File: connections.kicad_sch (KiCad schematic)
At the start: 37 parts, among them J1 Conn_01x01_Pin, J2 Conn_01x04_Pin, Q1 BSS138, Q2 BSS138

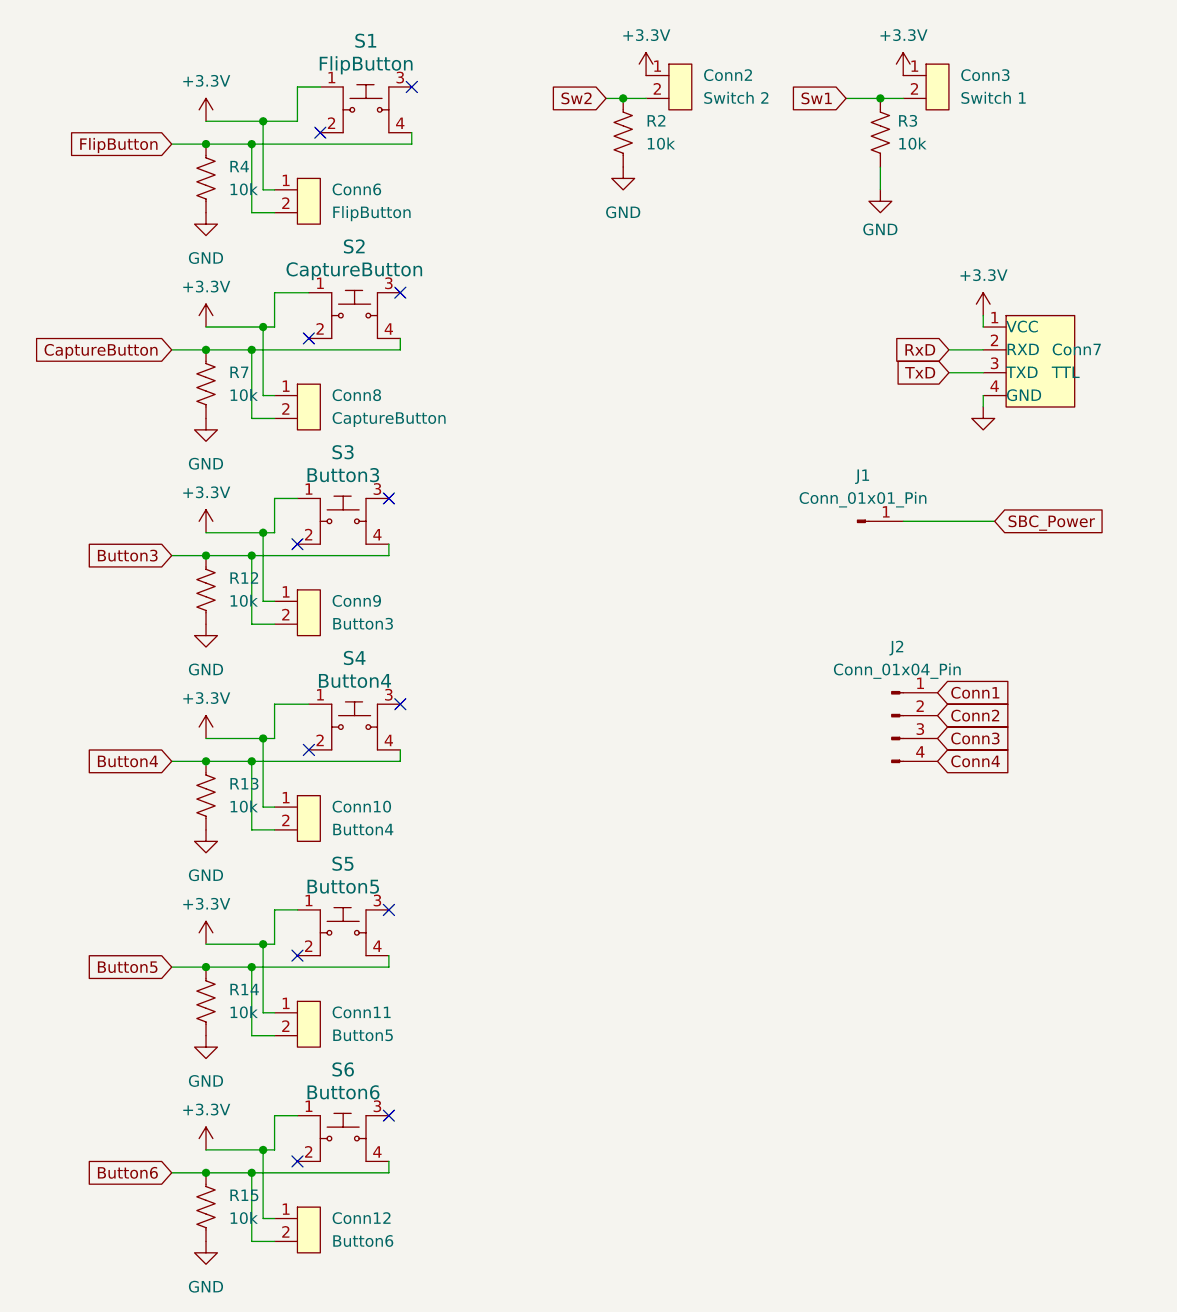
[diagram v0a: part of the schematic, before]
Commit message: Removed motor and added A4988
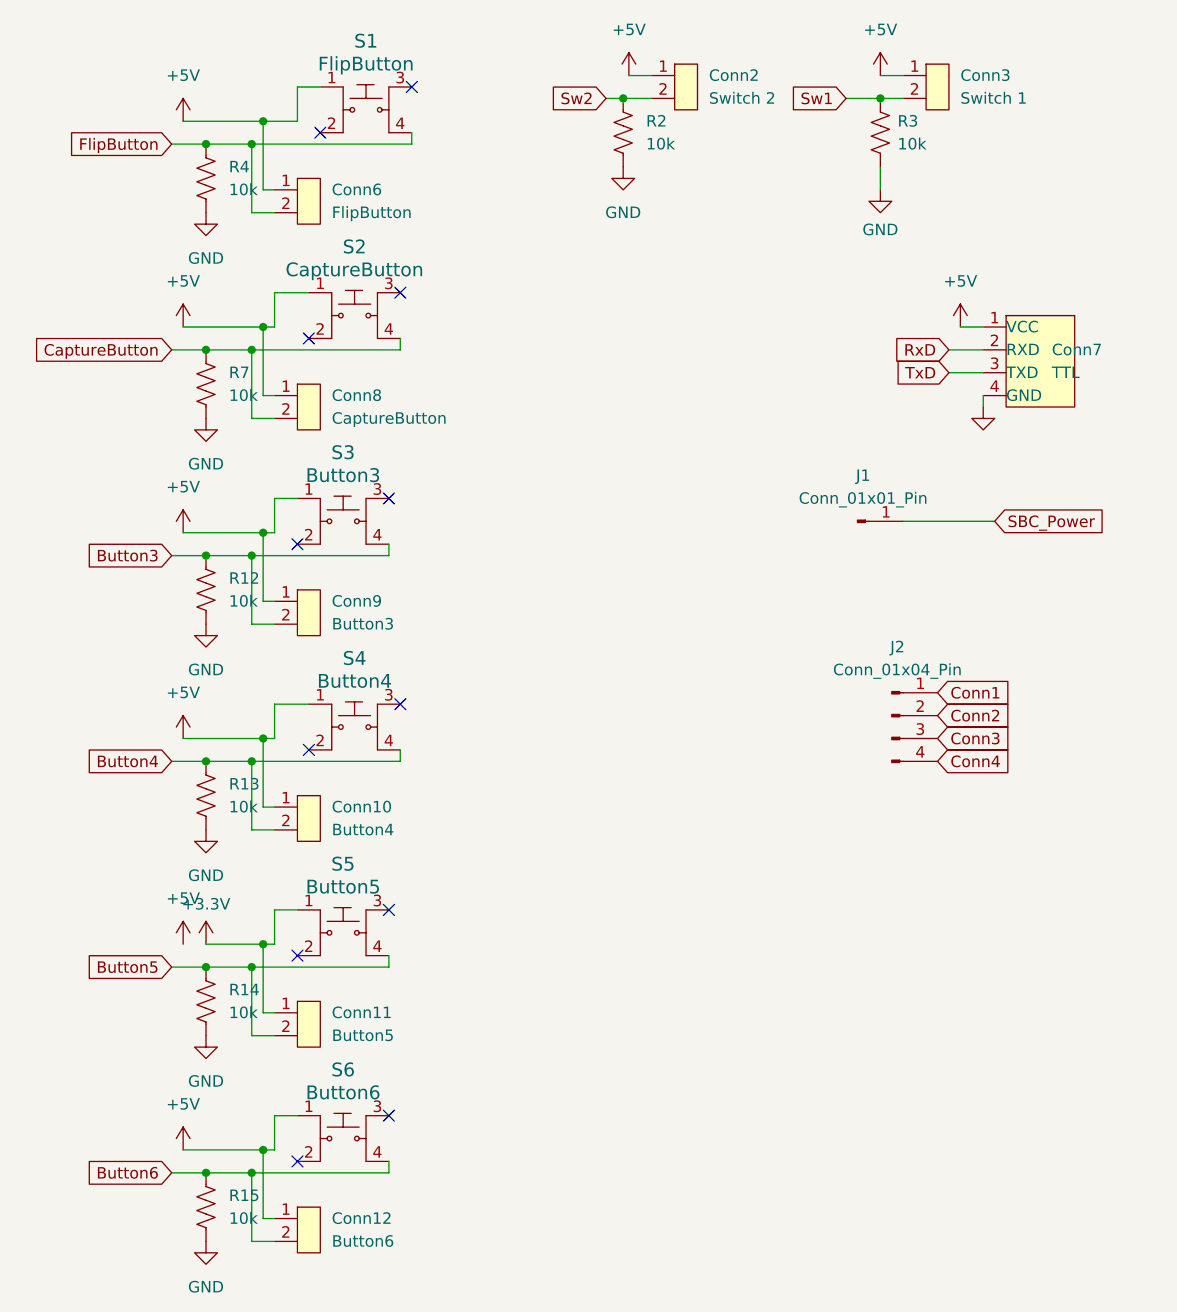
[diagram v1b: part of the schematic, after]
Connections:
- net +3.3V: no longer Conn10.1 (Pin_1), Conn12.1 (Pin_1), Conn2.1 (Pin_1), Conn3.1 (Pin_1), Conn6.1 (Pin_1), Conn7.1 (VCC), Conn8.1 (Pin_1), Conn9.1 (Pin_1), S1.1, S2.1, S3.1, S4.1, S6.1
- net +5V: now also Conn10.1 (Pin_1), Conn12.1 (Pin_1), Conn2.1 (Pin_1), Conn3.1 (Pin_1), Conn6.1 (Pin_1), Conn7.1 (VCC), Conn8.1 (Pin_1), Conn9.1 (Pin_1), S1.1, S2.1, S3.1, S4.1, S6.1
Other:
- moved on the sheet: Conn2

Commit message: Added motor driver
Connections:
- net +3.3V: no longer Conn11.1 (Pin_1), S5.1
- net +5V: now also Conn11.1 (Pin_1), S5.1
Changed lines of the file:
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@@
 	(wire
 		(pts
-			(xy 44.45 123.19) (xy 38.1 123.19)
-		)
-		(stroke
-			(width 0)
-			(type default)
-		)
-	)
-	(wire
-		(pts
 			(xy 43.18 80.01) (xy 43.18 87.63)
 		)
@@
 	(wire
 		(pts
+			(xy 38.1 123.19) (xy 44.45 123.19)
+		)
+		(stroke
+			(width 0)
+			(type default)
+		)
+	)
+	(wire
+		(pts
 			(xy 43.18 148.59) (xy 43.18 156.21)
 		)
@@
 	(symbol
 		(lib_id "power:+5V")
-		(at 35.56 123.19 0)
+		(at 38.1 123.19 0)
 		(unit 1)
 		(exclude_from_sim no)
@@
 		(fields_autoplaced yes)
 		(property "Reference" "#PWR057"
-			(at 35.56 127 0)
+			(at 38.1 127 0)
 			(effects
 				(font
@@
 		)
 		(property "Value" "+5V"
-			(at 35.56 118.11 0)
+			(at 38.1 118.11 0)
 			(effects
 				(font
@@
 		)
 		(property "Footprint" ""
-			(at 35.56 123.19 0)
+			(at 38.1 123.19 0)
 			(effects
 				(font
@@
 		)
 		(property "Datasheet" ""
-			(at 35.56 123.19 0)
+			(at 38.1 123.19 0)
 			(effects
 				(font
@@
 		)
 		(property "Description" ""
-			(at 35.56 123.19 0)
+			(at 38.1 123.19 0)
 			(effects
 				(font
@@
 					(unit 1)
 				)
-			)
-		)
-	)
-	(symbol
-		(lib_id "power:+3.3V")
-		(at 38.1 123.19 0)
-		(unit 1)
-		(exclude_from_sim no)
-		(in_bom yes)
-		(on_board yes)
-		(dnp no)
-		(fields_autoplaced yes)
-		(property "Reference" "#PWR030"
-			(at 38.1 127 0)
-			(effects
-				(font
-					(size 1.27 1.27)
-				)
-				(hide yes)
-			)
-		)
-		(property "Value" "+3.3V"
-			(at 38.1 118.745 0)
-			(effects
-				(font
-					(size 1.27 1.27)
-				)
-			)
-		)
-		(property "Footprint" ""
-			(at 38.1 123.19 0)
-			(effects
-				(font
-					(size 1.27 1.27)
-				)
-				(hide yes)
-			)
-		)
-		(property "Datasheet" ""
-			(at 38.1 123.19 0)
-			(effects
-				(font
-					(size 1.27 1.27)
-				)
-				(hide yes)
-			)
-		)
-		(property "Description" ""
-			(at 38.1 123.19 0)
-			(effects
-				(font
-					(size 1.27 1.27)
-				)
-				(hide yes)
-			)
-		)
-		(pin "1"
-		)
-		(instances
-			(project "Scout_Board"
-				(path "/e58a9779-147f-4c0c-a745-6e9bc8ec0357/1c50300d-eb18-4ae0-a965-4e91fdf6ec14"
-					(reference "#PWR030")
-					(unit 1)
-				)

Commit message: MID CHANGES
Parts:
- removed Conn2: Switch 2, Downloaded_footprints:CONN_B2B-ZRLFSN_JST, symbol Scout_library:B2B_VERT_1.5MM
- removed Conn3: Switch 1, Downloaded_footprints:CONN_B2B-ZRLFSN_JST, symbol Scout_library:B2B_VERT_1.5MM
- removed Conn4: TopLights, Downloaded_footprints:CONN_B2B-ZRLFSN_JST, symbol Scout_library:B2B_VERT_1.5MM
- removed Conn5: BottomLights, Downloaded_footprints:CONN_B2B-ZRLFSN_JST, symbol Scout_library:B2B_VERT_1.5MM
- added J10: P8, symbol Connector_Generic:Conn_02x13_Odd_Even
- added J7: Conn_02x07_Odd_Even, symbol Connector_Generic:Conn_02x07_Odd_Even
- added J9: P9, symbol Connector_Generic:Conn_02x13_Odd_Even
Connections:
- net +12V: now also J7.11 (Pin_11), J7.7 (Pin_7)
- net +5V: now also J7.3 (Pin_3), J7.4 (Pin_4)
- net Sw1: now also R2.1, J7.1 (Pin_1); no longer R3.1
- net Sw2: now also R3.1, J7.2 (Pin_2); no longer R2.1
- net BLa: now reaches MOSFET2.2 (D)
- net BLa: now also J7.9 (Pin_9)
- net TLa: now reaches MOSFET1.2 (D)
- net TLa: now also J7.5 (Pin_5)
- new net 1A: J7.8 (Pin_8)
- new net 1B: J7.6 (Pin_6)
- new net 2A: J7.10 (Pin_10)
- new net 2B: J7.12 (Pin_12)
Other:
- moved on the sheet: J2

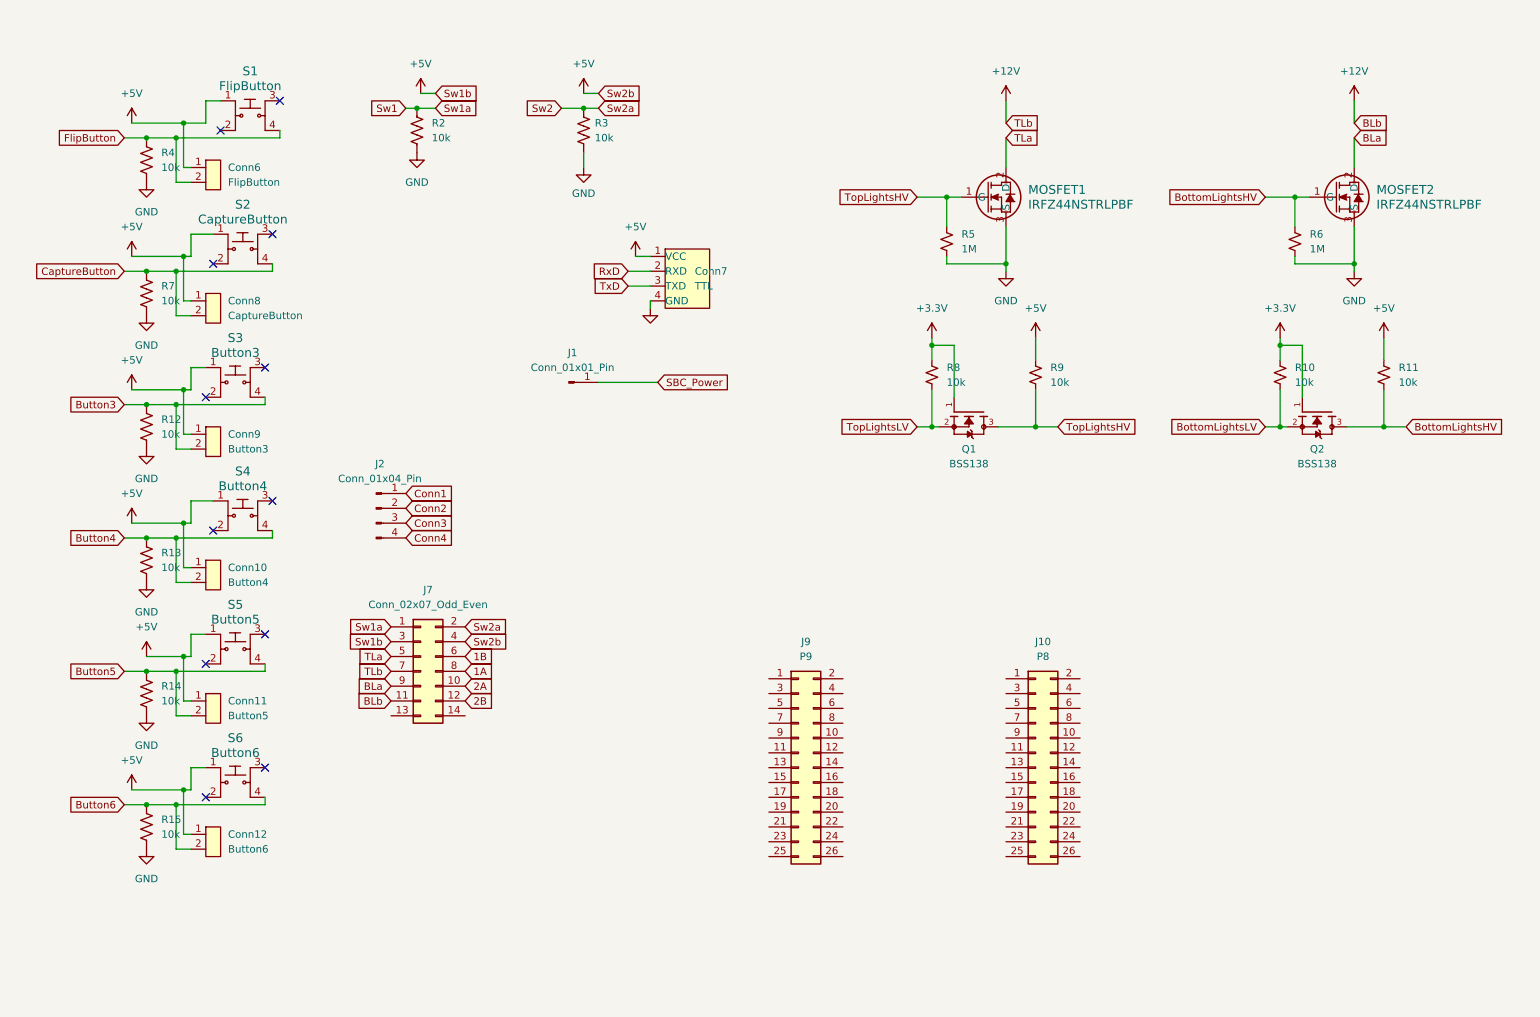
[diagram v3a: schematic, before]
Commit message: power board changes
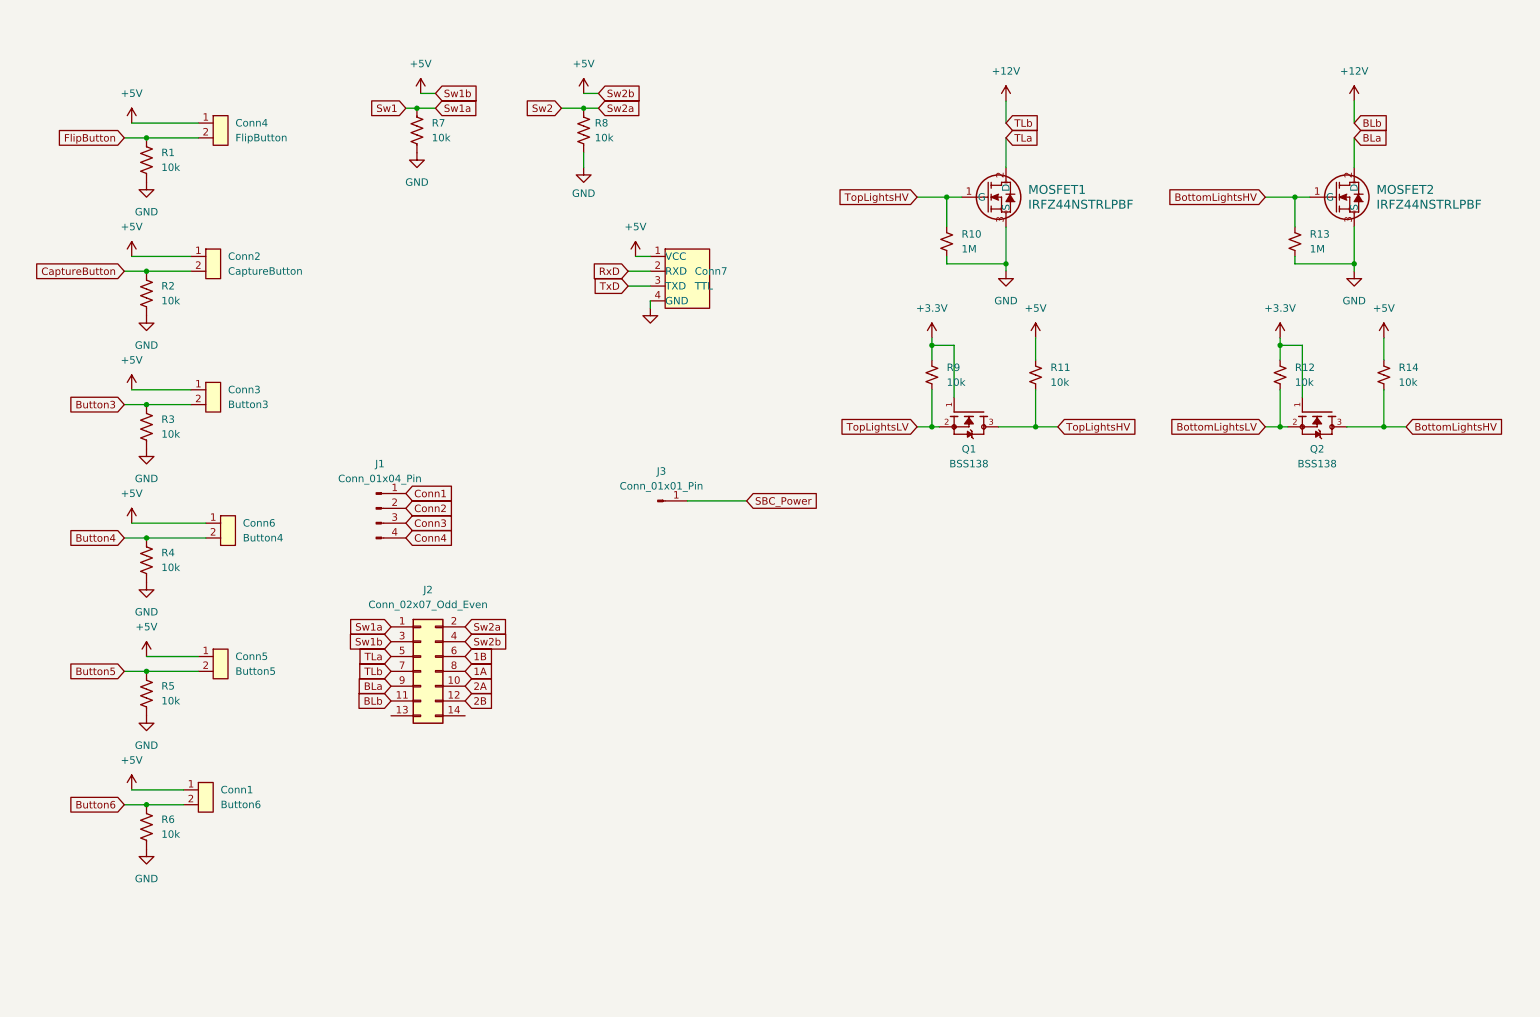
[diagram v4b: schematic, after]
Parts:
- removed J10: P8, symbol Connector_Generic:Conn_02x13_Odd_Even
- removed J9: P9, symbol Connector_Generic:Conn_02x13_Odd_Even
- removed S1: FlipButton, digikey-footprints:Switch_Tactile_SMD_4.5x4.5mm_TL3315NF160Q, symbol dk_Tactile-Switches:TL3315NF160Q
- removed S2: CaptureButton, digikey-footprints:Switch_Tactile_SMD_4.5x4.5mm_TL3315NF160Q, symbol dk_Tactile-Switches:TL3315NF160Q
- removed S3: Button3, digikey-footprints:Switch_Tactile_SMD_4.5x4.5mm_TL3315NF160Q, symbol dk_Tactile-Switches:TL3315NF160Q
- removed S4: Button4, digikey-footprints:Switch_Tactile_SMD_4.5x4.5mm_TL3315NF160Q, symbol dk_Tactile-Switches:TL3315NF160Q
- removed S5: Button5, digikey-footprints:Switch_Tactile_SMD_4.5x4.5mm_TL3315NF160Q, symbol dk_Tactile-Switches:TL3315NF160Q
- removed S6: Button6, digikey-footprints:Switch_Tactile_SMD_4.5x4.5mm_TL3315NF160Q, symbol dk_Tactile-Switches:TL3315NF160Q
- J2: renamed from J7; footprint (none) -> Connector_IDC:IDC-Header_2x07_P2.54mm_Vertical
- renumbered Conn12 to Conn1, Conn8 to Conn2, Conn9 to Conn3, Conn6 to Conn4, Conn11 to Conn5, Conn10 to Conn6, J2 to J1, J1 to J3, R4 to R1, R5 to R10, R9 to R11, R10 to R12, R6 to R13, R11 to R14, R7 to R2, R12 to R3, R13 to R4, R14 to R5, R15 to R6, R2 to R7, R3 to R8, R8 to R9
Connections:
- no-connect marks 12 -> 0
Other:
- moved on the sheet: Conn1, Conn2, Conn3, Conn4, Conn5, Conn6, J3

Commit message: New board test
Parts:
- removed Conn7: TTL, Downloaded_footprints:CONN_B4B-ZRLFSN_JST, symbol Scout_library:B4B_VERT_1.5MM
- Conn1, Conn2, Conn3, Conn4, Conn5, Conn6: footprint Downloaded_footprints:CONN_B2B-ZRLFSN_JST -> Connector_JST:JST_XH_B2B-XH-AM_1x02_P2.50mm_Vertical
- MOSFET1, MOSFET2: footprint Downloaded_footprints:D2PAK_INF -> IRFZ44NSTRLPBF:DPAK254P1524X483-3N
- Q1, Q2: footprint Downloaded_footprints:SOT95P240X111-3N -> BSS138:SOT95P240X111-3N

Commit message: Layout changes
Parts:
- removed J3: Conn_01x01_Pin, Connector_PinHeader_2.54mm:PinHeader_1x01_P2.54mm_Vertical, symbol Connector:Conn_01x01_Pin
- added MOSFET3: IRFZ44NSTRLPBF, IRFZ44NSTRLPBF:DPAK254P1524X483-3N, symbol 2024-05-21_14-07-33:IRFZ44NSTRLPBF
- added Q3: BSS138, BSS138:SOT95P240X111-3N, symbol BSS138:BSS138
- added R29, R31: 10k, Resistor_SMD:R_0603_1608Metric_Pad0.98x0.95mm_HandSolder, symbol Device:R_Small_US
- added R30: 1M, Resistor_SMD:R_0603_1608Metric_Pad0.98x0.95mm_HandSolder, symbol Device:R_Small_US
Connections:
- net +12V: now also J2.5 (Pin_5); no longer J2.11 (Pin_11)
- net +3.3V: now also Q3.1, R29.1
- net +5V: now also R31.1
- net GND: now also MOSFET3.3 (S), R30.2
- net BLa: no longer names the net of J2.9 (Pin_9)
- net BLa: no longer MOSFET2.2 (D)
- net TLa renamed TL-
- net TL-: no longer J2.5 (Pin_5)
- new net BL-: MOSFET2.2 (D)
- new net UV-: MOSFET3.2 (D)
- new net UVLightsHV: MOSFET3.1 (G), Q3.3, R30.1, R31.2
- new net UVLightsLV: Q3.2, R29.2

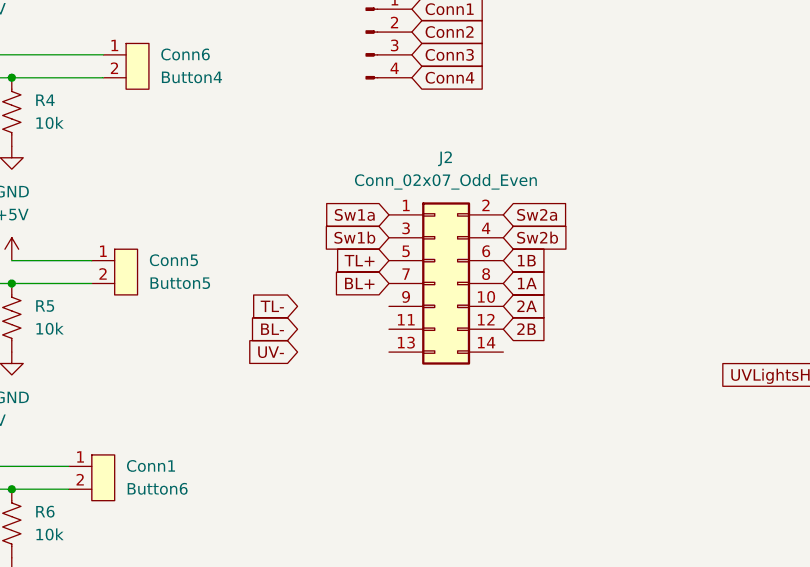
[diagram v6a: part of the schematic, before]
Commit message: Layout updated with mounting holes
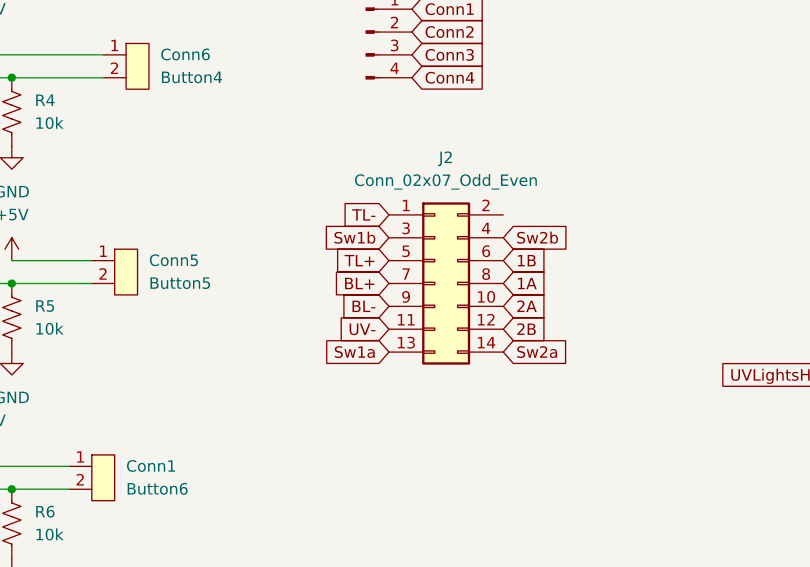
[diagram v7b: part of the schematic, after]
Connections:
- net BL-: now also J2.9 (Pin_9)
- net Sw1: now also J2.13 (Pin_13); no longer J2.1 (Pin_1)
- net Sw2: now also J2.14 (Pin_14); no longer J2.2 (Pin_2)
- net TL-: now also J2.1 (Pin_1)
- net UV-: now also J2.11 (Pin_11)
